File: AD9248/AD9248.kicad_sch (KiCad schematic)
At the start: 1 part, among them U1 AD9284BCPZ-250

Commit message: Power supply started
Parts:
- removed U1: AD9284BCPZ-250, CP_48_12_ADI, symbol 2026-10-21_18-41-16:AD9284BCPZ-250
- added C1, C2, C3: GCM188R71E105KA64D, CAP_GCM188_MUR, symbol GCM188R71E105KA64D:GCM188R71E105KA64D
- added C4, C5, C6: C0603C104K5RACTU, CAPC17595_95N_KEM, symbol C0603C104K5RACTU:C0603C104K5RACTU
- added J1, J2: Conn_01x01_Pin, symbol Connector:Conn_01x01_Pin
- added U1, U3: TLV70018DCKR, DCK5, symbol TLV70018DCKR:TLV70018DCKR
- added U2: AD9284BCPZ-250, CP_48_12_ADI, symbol AD9248:AD9284BCPZ-250
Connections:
- new net GND: C1.1, C4.1, C5.1, C6.1, J2.1 (Pin_1), U1.2 (GND), U2.28 (DRGND), U2.7 (DRGND), U3.2 (GND)
- new net VCC_Analog: C2.2, C4.2, C5.2, C6.2, U1.5 (OUT), U2.1 (AVDD), U2.2 (AVDD), U2.35 (AVDD), U2.36 (AVDD), U2.37 (AVDD), U2.44 (AVDD), U2.45 (AVDD)
- new net VCC_Digital: C3.2, U3.5 (OUT)
- new net VCC_Raw: C1.2, C2.1, C3.1, J1.1 (Pin_1), U1.1 (IN), U1.3 (EN), U3.1 (IN), U3.3 (EN)
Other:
- note added: "0.1u"
- note added: "1uF"
- note added: "< 6V Input, ground plane required"
- note added: "POWER SUPPLY"
- note added: "pin 1, 2"
- note added: "pin 35 - 37"
- note added: "pin 44, 45"

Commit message: Power Supply Schematic Portion Complete
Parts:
- added C7, C8, C9: C0603C104K5RACTU, part_library:C0603C104K5RACTU, symbol C0603C104K5RACTU:C0603C104K5RACTU
- C1, C2, C3: footprint CAP_GCM188_MUR -> part_library:GCM188R71E105KA64D
- C4, C5, C6: footprint CAPC17595_95N_KEM -> part_library:C0603C104K5RACTU
- U1, U3: footprint DCK5 -> part_library:TLV70018DCKR
- U2: footprint CP_48_12_ADI -> part_library:AD9284
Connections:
- net GND: now also C2.1, C3.1, U2.HTAB (EPAD), C7.1, C8.1, C9.1
- net VCC_Analog: now also U2.42 (AVDD), U2.48 (AVDD), C7.2
- net VCC_Digital: now also U2.27 (DRVDD), U2.8 (DRVDD), C8.2, C9.2
- net VCC_Raw: no longer C2.1, C3.1
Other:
- note added: "*Note: we may need to add a .1uF pair to each of these (see eval board schematic)"
- note added: "C0603C104K5RACTU"
- note added: "Pin 8"
- note added: "pin 27"
- note added: "pin 42"
- note added: "pin 44, 45, 48"
- note removed: "pin 44, 45"
- moved on the sheet: C1, C2, C3, C4, C5, C6, J1, J2, U1, U3

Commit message: Schematic for ADC breakout complete (ish)
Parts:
- removed C1, C2, C3: GCM188R71E105KA64D, part_library:GCM188R71E105KA64D, symbol GCM188R71E105KA64D:GCM188R71E105KA64D
- removed C4, C5, C6, C7, C8, C9: C0603C104K5RACTU, part_library:C0603C104K5RACTU, symbol C0603C104K5RACTU:C0603C104K5RACTU
- removed J1, J2: Conn_01x01_Pin, symbol Connector:Conn_01x01_Pin
- removed U1, U3: TLV70018DCKR, part_library:TLV70018DCKR, symbol TLV70018DCKR:TLV70018DCKR
- removed U2: AD9284BCPZ-250, part_library:AD9284, symbol AD9248:AD9284BCPZ-250
- added J1, J2, J3, J4: CON292001-1, part_library:TE_CON292001-1, symbol CON292001-1:CON292001-1
- added U4, U5, U6, U7: PPPC062LJBN-RC, part_library:CONN_PPPC062LJBN-RC_SUL, symbol PPPC062LJBN_RC:PPPC062LJBN-RC
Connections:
- net GND: now also U4.2, U4.8, U5.2, U5.8, U6.2, U6.8, U7.2, U7.8
- net VCC_Raw: now also U4.1, U4.7, U5.1, U5.7, U6.1, U6.7, U7.1, U7.7
- new net ADC_unit/ADAR_VIN_1_N: J1.2, J1.3, J1.4
- new net ADC_unit/ADAR_VIN_1_P: J1.1
- new net ADC_unit/ADAR_VIN_2_N: J2.2, J2.3, J2.4
- new net ADC_unit/ADAR_VIN_2_P: J2.1
- new net ADC_unit1/ADAR_VIN_1_N: J3.2, J3.3, J3.4
- new net ADC_unit1/ADAR_VIN_1_P: J3.1
- new net ADC_unit1/ADAR_VIN_2_N: J4.2, J4.3, J4.4
- new net ADC_unit1/ADAR_VIN_2_P: J4.1
- new net FPGA_CLK: U6.3
- new net FPGA_SPI_CLK: U6.12
- new net FPGA_SPI_CS_ADC1: U6.11
- new net FPGA_SPI_CS_ADC2: U6.10
- new net FPGA_SPI_MOSI: U6.9
- new net PMOD_ADC0: U4.3
- new net PMOD_ADC0_2: U5.3
- new net PMOD_ADC1: U4.4
- new net PMOD_ADC1_2: U5.4
- new net PMOD_ADC2: U4.5
- new net PMOD_ADC2_2: U5.5
- new net PMOD_ADC3: U4.6
- new net PMOD_ADC3_2: U5.6
- new net PMOD_ADC4: U4.9
- new net PMOD_ADC4_2: U5.9
- new net PMOD_ADC5: U4.10
- new net PMOD_ADC5_2: U5.10
- new net PMOD_ADC6: U4.11
- new net PMOD_ADC6_2: U5.11
- new net PMOD_ADC7: U4.12
- new net PMOD_ADC7_2: U5.12
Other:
- added sheet ADC_unit (ADC_unit.kicad_sch)
- added sheet ADC_unit1 (ADC_unit.kicad_sch)
- note added: "CONNECTORS"
- note removed: "*Note: we may need to add a .1uF pair to each of these (see eval board schematic)"
- note removed: "0.1u"
- note removed: "1uF"
- note removed: "< 6V Input, ground plane required"
- note removed: "C0603C104K5RACTU"
- note removed: "POWER SUPPLY"
- note removed: "Pin 8"
- note removed: "pin 1, 2"
- note removed: "pin 27"
- note removed: "pin 35 - 37"
- note removed: "pin 42"
- note removed: "pin 44, 45, 48"

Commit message: Schematic under construction - clock / analog input driver defered but digital outputs are now wired correctly with correct differential impedance
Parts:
- removed J1, J2, J3, J4: CON292001-1, part_library:TE_CON292001-1, symbol CON292001-1:CON292001-1
- removed U5, U7: PPPC062LJBN-RC, part_library:CONN_PPPC062LJBN-RC_SUL, symbol PPPC062LJBN_RC:PPPC062LJBN-RC
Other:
- removed sheet ADC_unit1
- added sheet References (References.kicad_sch)
- note added: "BASYS 3 FPGA to AD9248 connectors (PMOD)"
- note removed: "CONNECTORS"
- moved on the sheet: U4, U6

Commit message: Rough draft completete, TODO: Cosmetic stuff (Make it more modular in schematic), simulate sallen key with non-ideal components, check FPGA pinout constraints for clock generation, validate design
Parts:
- removed U4, U6: PPPC062LJBN-RC, part_library:CONN_PPPC062LJBN-RC_SUL, symbol PPPC062LJBN_RC:PPPC062LJBN-RC
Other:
- removed sheet ADC_unit
- added sheet Top Level (top_level.kicad_sch)
- note added: "(1)"
- note added: "(2)"
- note added: "(3)"
- note added: "(4)"
- note added: "(5)"
- note added: "Table of contents"
- note removed: "BASYS 3 FPGA to AD9248 connectors (PMOD)"
- company: (none) -> SD26-11 - Aidan O'Grady
- title: (none) -> Table of Contents

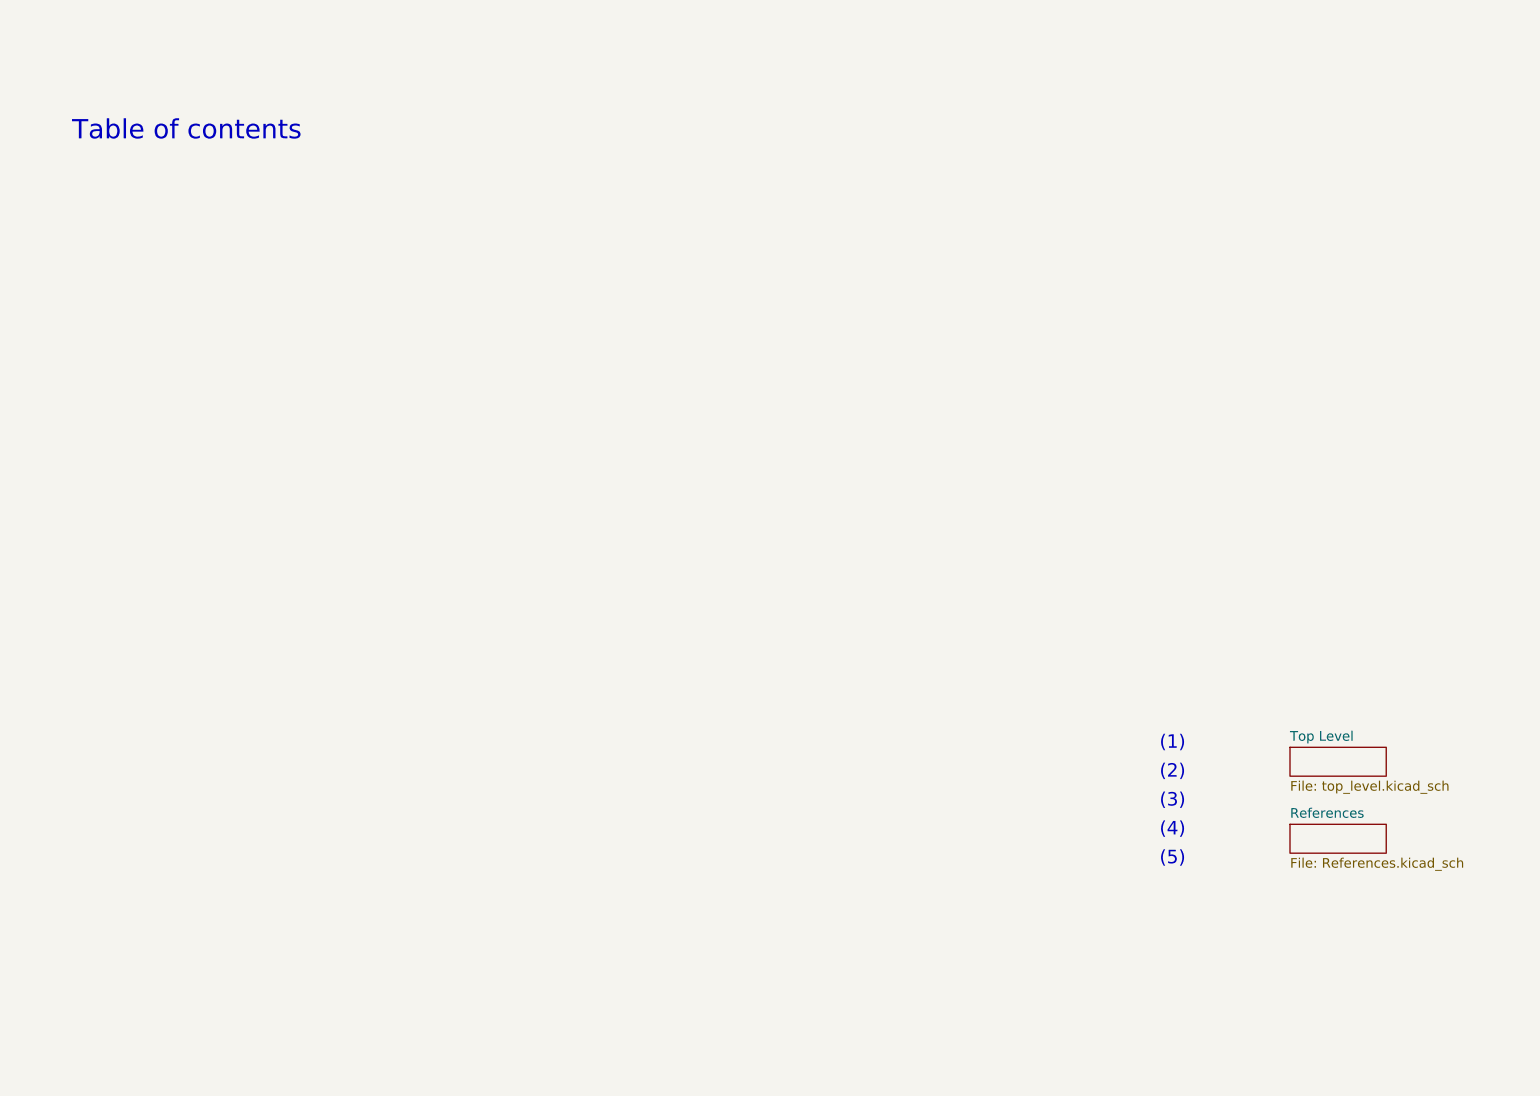
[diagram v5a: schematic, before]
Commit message: Finished and reviewed schematic, one change so far needs to be made: OE pin on level shifters must be externally toggled instead of tied to VCC. The IC requires VDDA/B to be fully ramped before pulling the OE high.
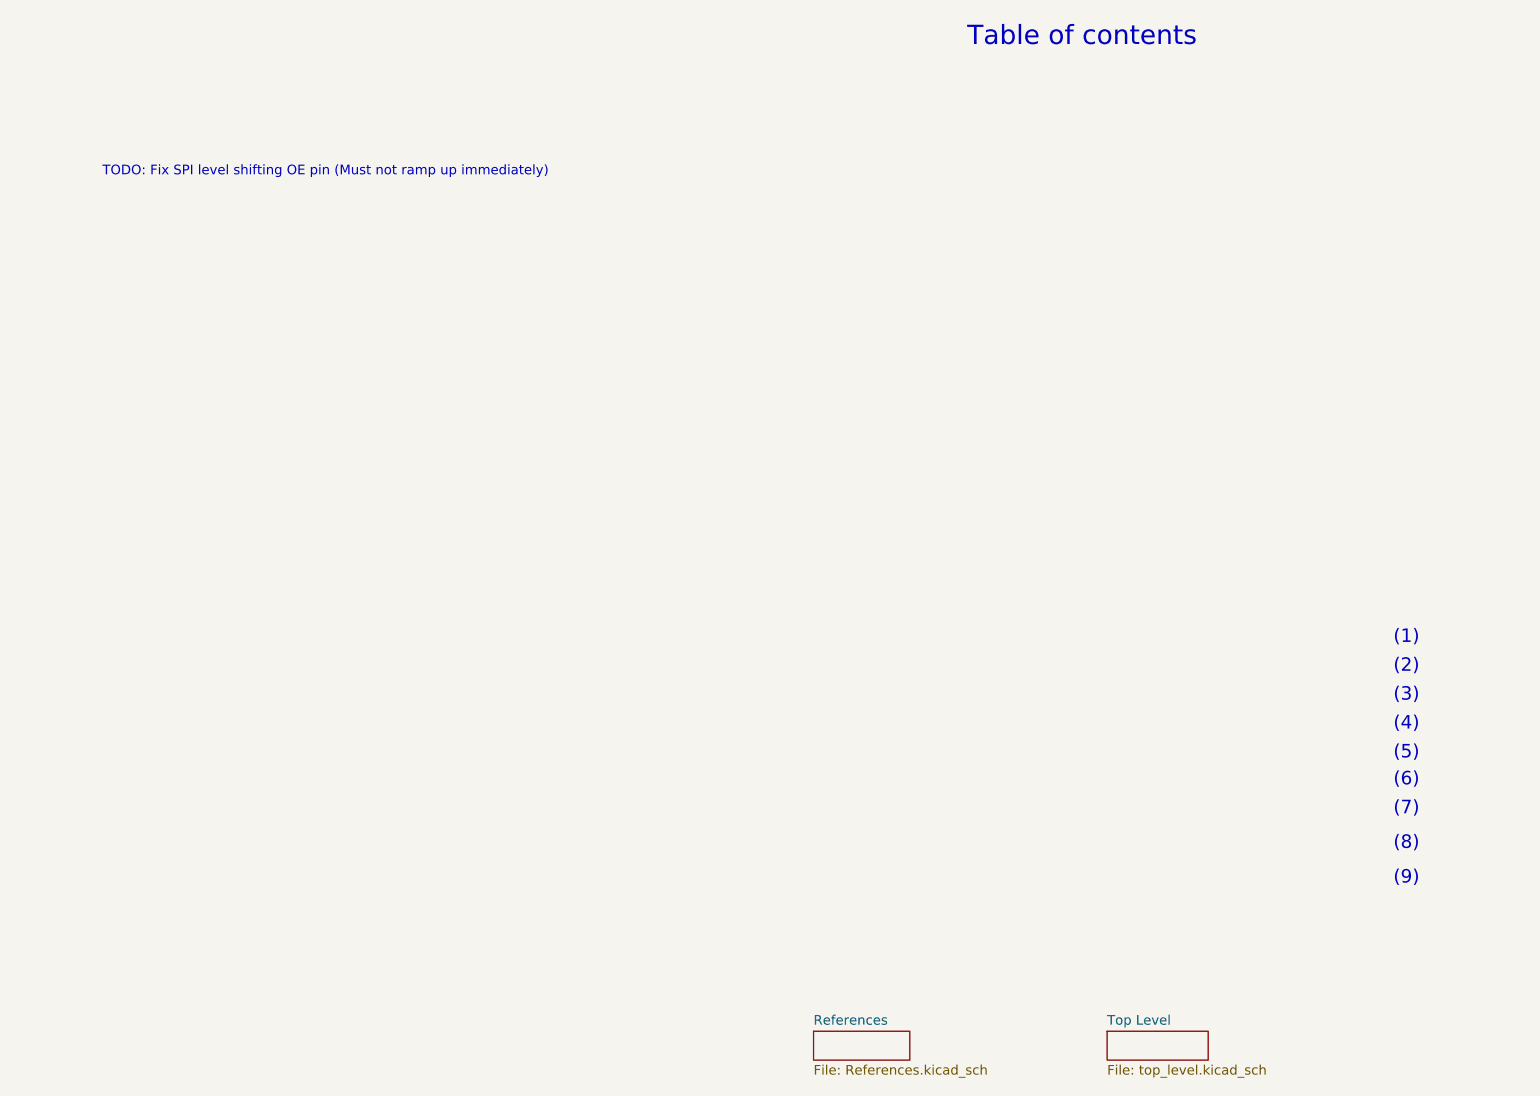
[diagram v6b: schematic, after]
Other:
- note added: "(6)"
- note added: "(7)"
- note added: "(8)"
- note added: "(9)"
- note added: "TODO: Fix SPI level shifting OE pin (Must not ramp up immediately)"
